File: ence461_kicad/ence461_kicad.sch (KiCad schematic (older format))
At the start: 47 parts, among them U1 LMV324, U2 LMV324, U3 LMV324, U4 74HC3G14DP, U5 LMV321

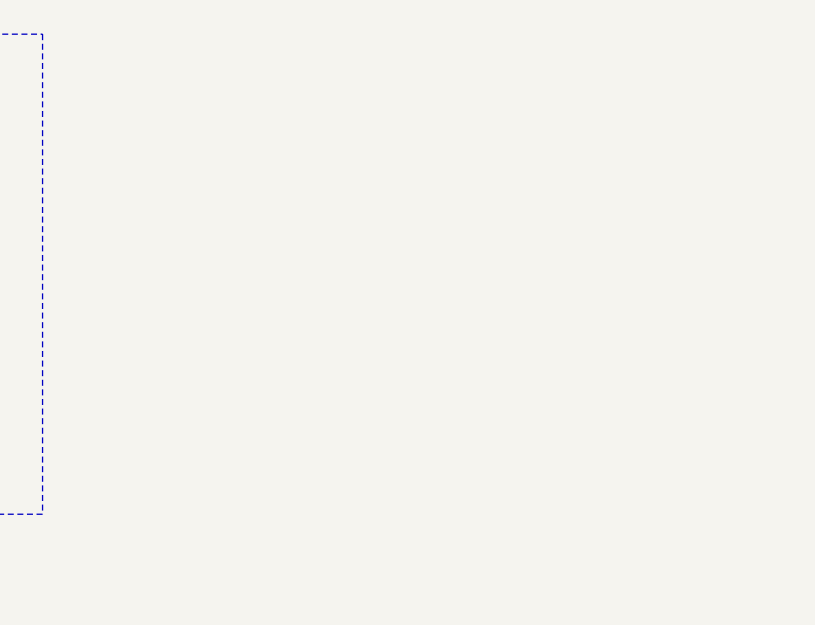
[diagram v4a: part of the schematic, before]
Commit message: Added TPS717 symbol to schematic.
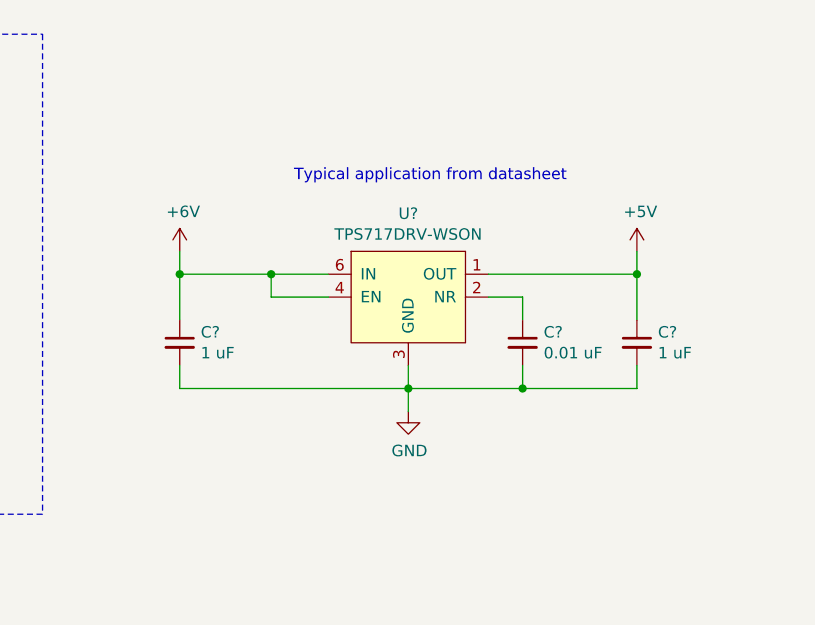
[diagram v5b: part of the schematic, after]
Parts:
- added C?: 0.01 uF, symbol Device:C_Small
- added C? (x2): 1 uF, symbol Device:C_Small
- added U?: TPS717DRV-WSON, Package_SON:WSON-6-1EP_2x2mm_P0.65mm_EP1x1.6mm_ThermalVias, symbol ence461_symbol_library:TPS717DRV-WSON
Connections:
- net +5V: now also C?.1, U?.1 (OUT)
- net GND: now also C?.2, C?.2, C?.2, U?.3 (GND)
- new net: C?.1, U?.2 (NR)
- new net +6V: C?.1, U?.4 (EN), U?.6 (IN)
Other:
- note added: "Typical application from datasheet"
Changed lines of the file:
@@
 Text Notes 3350 11050 0    101  ~ 0
 CAN Transceiver Circuit
+$Comp
+L ence461_symbol_library:TPS717DRV-WSON U?
+U 1 1 5F0550EF
+P 8000 9950
+F 0 "U?" H 8000 10065 50  0000 C CNN
+F 1 "TPS717DRV-WSON" H 8000 9974 50  0000 C CNN
+F 2 "Package_SON:WSON-6-1EP_2x2mm_P0.65mm_EP1x1.6mm_ThermalVias" H 8000 9950 50  0001 C CNN
+F 3 "http://www.ti.com/lit/ds/symlink/tps717.pdf?HQS=TI-null-null-digikeymode-df-pf-null-wwe&ts=1590186425971" H 8000 9950 50  0001 C CNN
+	1    8000 9950
+	1    0    0    -1
+$EndComp
+$Comp
+L power:GND #PWR?
+U 1 1 5F0554ED
+P 8000 10700
+F 0 "#PWR?" H 8000 10450 50  0001 C CNN
+F 1 "GND" H 8005 10527 50  0000 C CNN
+F 2 "" H 8000 10700 50  0001 C CNN
+F 3 "" H 8000 10700 50  0001 C CNN
+	1    8000 10700
+	1    0    0    -1
+$EndComp
+$Comp
+L Device:C_Small C?
+U 1 1 5F05E77E
+P 8500 10400
+F 0 "C?" H 8592 10446 50  0000 L CNN
+F 1 "0.01 uF" H 8592 10355 50  0000 L CNN
+F 2 "" H 8500 10400 50  0001 C CNN
+F 3 "~" H 8500 10400 50  0001 C CNN
+	1    8500 10400
+	1    0    0    -1
+$EndComp
+$Comp
+L Device:C_Small C?
+U 1 1 5F05EC29
+P 7000 10400
+F 0 "C?" H 7092 10446 50  0000 L CNN
+F 1 "1 uF" H 7092 10355 50  0000 L CNN
+F 2 "" H 7000 10400 50  0001 C CNN
+F 3 "~" H 7000 10400 50  0001 C CNN
+	1    7000 10400
+	1    0    0    -1
+$EndComp
+$Comp
+L Device:C_Small C?
+U 1 1 5F05F1F3
+P 9000 10400
+F 0 "C?" H 9092 10446 50  0000 L CNN
+F 1 "1 uF" H 9092 10355 50  0000 L CNN
+F 2 "" H 9000 10400 50  0001 C CNN
+F 3 "~" H 9000 10400 50  0001 C CNN
+	1    9000 10400
+	1    0    0    -1
+$EndComp
+Wire Wire Line
+	8350 10200 8500 10200
+Wire Wire Line
+	8500 10200 8500 10300
+Wire Wire Line
+	8350 10100 9000 10100
+Wire Wire Line
+	8000 10500 8000 10600
+Wire Wire Line
+	8000 10600 8500 10600
+Wire Wire Line
+	8500 10600 8500 10500
+Connection ~ 8000 10600
+Wire Wire Line
+	8000 10600 8000 10700
+Wire Wire Line
+	8500 10600 9000 10600
+Connection ~ 8500 10600
+Wire Wire Line
+	8000 10600 7000 10600
+Wire Wire Line
+	7000 10600 7000 10500
+Wire Wire Line
+	7650 10100 7400 10100
+Wire Wire Line
+	7000 10100 7000 10300
+Wire Wire Line
+	9000 10500 9000 10600
+Wire Wire Line
+	9000 10300 9000 10100
+Wire Wire Line
+	7650 10200 7400 10200
+Wire Wire Line
+	7400 10200 7400 10100
+Connection ~ 7400 10100
+Wire Wire Line
+	7400 10100 7000 10100
+$Comp
+L power:+6V #PWR?
+U 1 1 5F0FB207
+P 7000 10000
+F 0 "#PWR?" H 7000 9850 50  0001 C CNN
+F 1 "+6V" H 7015 10173 50  0000 C CNN
+F 2 "" H 7000 10000 50  0001 C CNN
+F 3 "" H 7000 10000 50  0001 C CNN
+	1    7000 10000
+	1    0    0    -1
+$EndComp
+$Comp
+L power:+5V #PWR?
+U 1 1 5F0FB4D8
+P 9000 10000
+F 0 "#PWR?" H 9000 9850 50  0001 C CNN
+F 1 "+5V" H 9015 10173 50  0000 C CNN
+F 2 "" H 9000 10000 50  0001 C CNN
+F 3 "" H 9000 10000 50  0001 C CNN
+	1    9000 10000
+	1    0    0    -1
+$EndComp
+Wire Wire Line
+	9000 10000 9000 10100
+Connection ~ 9000 10100
+Wire Wire Line
+	7000 10000 7000 10100
+Connection ~ 7000 10100
+Text Notes 7500 9700 0    50   ~ 0
+Typical application from datasheet
 $EndSCHEMATC

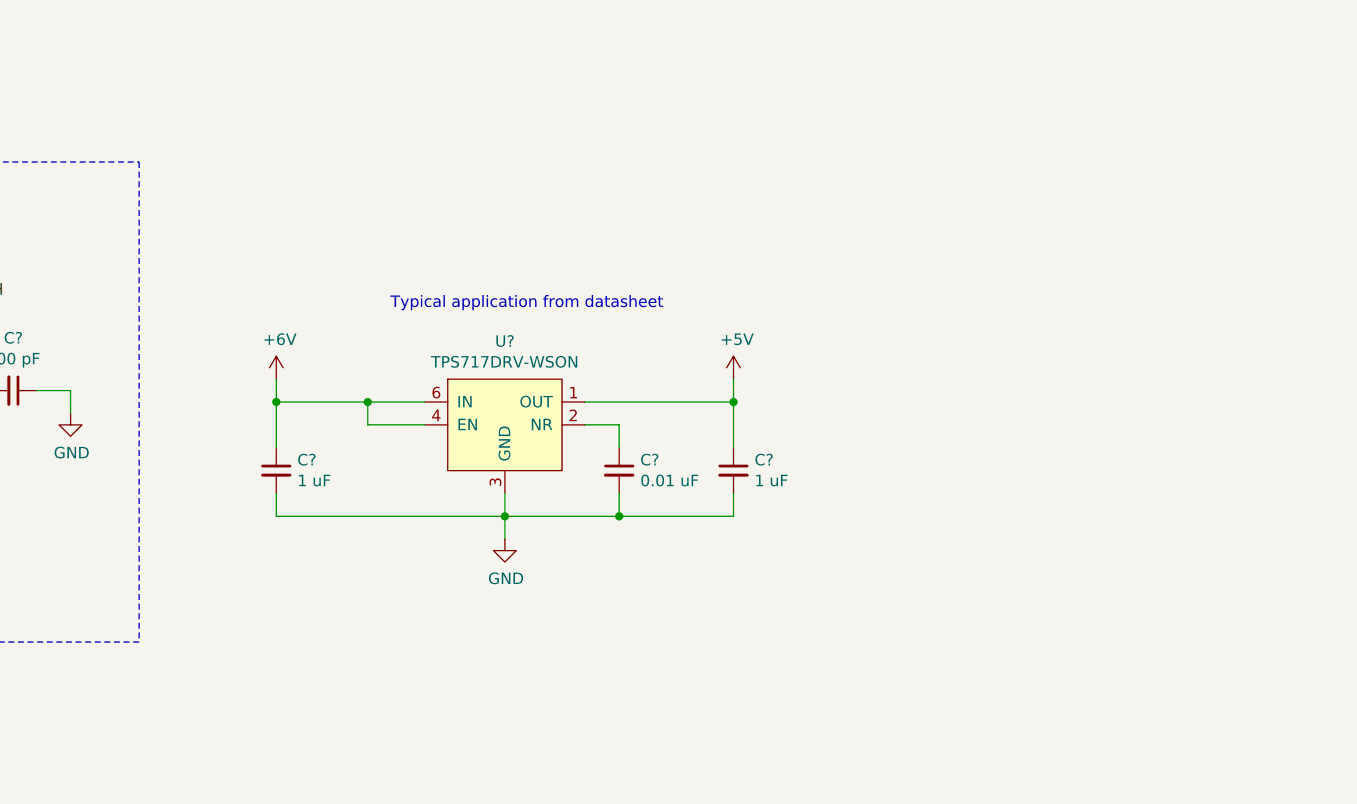
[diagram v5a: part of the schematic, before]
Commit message: Added TPS714 supply.
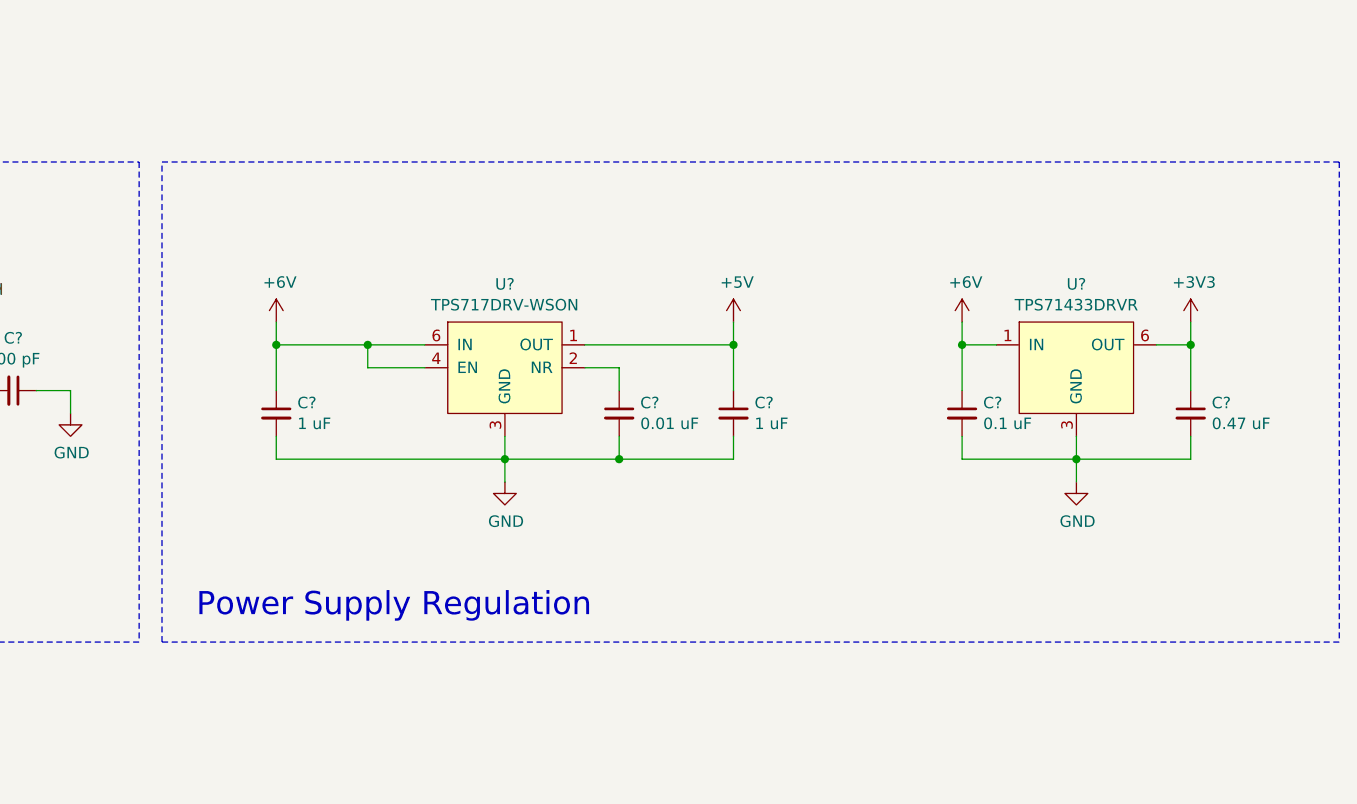
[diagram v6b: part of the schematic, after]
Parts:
- added C?: 0.1 uF, symbol Device:C_Small
- added C?: 0.47 uF, symbol Device:C_Small
- added U?: TPS71433DRVR, Package_SON:WSON-6-1EP_2x2mm_P0.65mm_EP1x1.6mm, symbol ence461_symbol_library:TPS71433DRVR
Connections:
- net +3V3: now also C?.1, U?.6 (OUT)
- net +6V: now also C?.1, U?.1 (IN)
- net GND: now also C?.2, C?.2, U?.3 (GND)
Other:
- note added: "Power Supply Regulation"
- note removed: "Typical application from datasheet"
- moved on the sheet: C?, U?
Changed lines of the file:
@@
 L ence461_symbol_library:TPS717DRV-WSON U?
 U 1 1 5F0550EF
-P 8000 9950
-F 0 "U?" H 8000 10065 50  0000 C CNN
-F 1 "TPS717DRV-WSON" H 8000 9974 50  0000 C CNN
-F 2 "Package_SON:WSON-6-1EP_2x2mm_P0.65mm_EP1x1.6mm_ThermalVias" H 8000 9950 50  0001 C CNN
-F 3 "http://www.ti.com/lit/ds/symlink/tps717.pdf?HQS=TI-null-null-digikeymode-df-pf-null-wwe&ts=1590186425971" H 8000 9950 50  0001 C CNN
-	1    8000 9950
+P 8000 9700
+F 0 "U?" H 8000 9815 50  0000 C CNN
+F 1 "TPS717DRV-WSON" H 8000 9724 50  0000 C CNN
+F 2 "Package_SON:WSON-6-1EP_2x2mm_P0.65mm_EP1x1.6mm_ThermalVias" H 8000 9700 50  0001 C CNN
+F 3 "http://www.ti.com/lit/ds/symlink/tps717.pdf?HQS=TI-null-null-digikeymode-df-pf-null-wwe&ts=1590186425971" H 8000 9700 50  0001 C CNN
+	1    8000 9700
 	1    0    0    -1
 $EndComp
@@
 L power:GND #PWR?
 U 1 1 5F0554ED
-P 8000 10700
-F 0 "#PWR?" H 8000 10450 50  0001 C CNN
-F 1 "GND" H 8005 10527 50  0000 C CNN
-F 2 "" H 8000 10700 50  0001 C CNN
-F 3 "" H 8000 10700 50  0001 C CNN
-	1    8000 10700
+P 8000 10450
+F 0 "#PWR?" H 8000 10200 50  0001 C CNN
+F 1 "GND" H 8005 10277 50  0000 C CNN
+F 2 "" H 8000 10450 50  0001 C CNN
+F 3 "" H 8000 10450 50  0001 C CNN
+	1    8000 10450
 	1    0    0    -1
 $EndComp
@@
 L Device:C_Small C?
 U 1 1 5F05E77E
-P 8500 10400
-F 0 "C?" H 8592 10446 50  0000 L CNN
-F 1 "0.01 uF" H 8592 10355 50  0000 L CNN
-F 2 "" H 8500 10400 50  0001 C CNN
-F 3 "~" H 8500 10400 50  0001 C CNN
-	1    8500 10400
+P 8500 10150
+F 0 "C?" H 8592 10196 50  0000 L CNN
+F 1 "0.01 uF" H 8592 10105 50  0000 L CNN
+F 2 "" H 8500 10150 50  0001 C CNN
+F 3 "~" H 8500 10150 50  0001 C CNN
+	1    8500 10150
 	1    0    0    -1
 $EndComp
@@
 L Device:C_Small C?
 U 1 1 5F05EC29
-P 7000 10400
-F 0 "C?" H 7092 10446 50  0000 L CNN
-F 1 "1 uF" H 7092 10355 50  0000 L CNN
-F 2 "" H 7000 10400 50  0001 C CNN
-F 3 "~" H 7000 10400 50  0001 C CNN
-	1    7000 10400
+P 7000 10150
+F 0 "C?" H 7092 10196 50  0000 L CNN
+F 1 "1 uF" H 7092 10105 50  0000 L CNN
+F 2 "" H 7000 10150 50  0001 C CNN
+F 3 "~" H 7000 10150 50  0001 C CNN
+	1    7000 10150
 	1    0    0    -1
 $EndComp
@@
 L Device:C_Small C?
 U 1 1 5F05F1F3
-P 9000 10400
-F 0 "C?" H 9092 10446 50  0000 L CNN
-F 1 "1 uF" H 9092 10355 50  0000 L CNN
-F 2 "" H 9000 10400 50  0001 C CNN
-F 3 "~" H 9000 10400 50  0001 C CNN
-	1    9000 10400
-	1    0    0    -1
-$EndComp
-Wire Wire Line
-	8350 10200 8500 10200
-Wire Wire Line
-	8500 10200 8500 10300
-Wire Wire Line
-	8350 10100 9000 10100
-Wire Wire Line
-	8000 10500 8000 10600
-Wire Wire Line
-	8000 10600 8500 10600
-Wire Wire Line
-	8500 10600 8500 10500
-Connection ~ 8000 10600
-Wire Wire Line
-	8000 10600 8000 10700
-Wire Wire Line
-	8500 10600 9000 10600
-Connection ~ 8500 10600
-Wire Wire Line
-	8000 10600 7000 10600
-Wire Wire Line
-	7000 10600 7000 10500
-Wire Wire Line
-	7650 10100 7400 10100
-Wire Wire Line
-	7000 10100 7000 10300
-Wire Wire Line
-	9000 10500 9000 10600
-Wire Wire Line
-	9000 10300 9000 10100
-Wire Wire Line
-	7650 10200 7400 10200
-Wire Wire Line
-	7400 10200 7400 10100
-Connection ~ 7400 10100
-Wire Wire Line
-	7400 10100 7000 10100
+P 9000 10150
+F 0 "C?" H 9092 10196 50  0000 L CNN
+F 1 "1 uF" H 9092 10105 50  0000 L CNN
+F 2 "" H 9000 10150 50  0001 C CNN
+F 3 "~" H 9000 10150 50  0001 C CNN
+	1    9000 10150
+	1    0    0    -1
+$EndComp
+Wire Wire Line
+	8350 9950 8500 9950
+Wire Wire Line
+	8500 9950 8500 10050
+Wire Wire Line
+	8350 9850 9000 9850
+Wire Wire Line
+	8000 10250 8000 10350
+Wire Wire Line
+	8000 10350 8500 10350
+Wire Wire Line
+	8500 10350 8500 10250
+Connection ~ 8000 10350
+Wire Wire Line
+	8000 10350 8000 10450
+Wire Wire Line
+	8500 10350 9000 10350
+Connection ~ 8500 10350
+Wire Wire Line
+	8000 10350 7000 10350
+Wire Wire Line
+	7000 10350 7000 10250
+Wire Wire Line
+	7650 9850 7400 9850
+Wire Wire Line
+	7000 9850 7000 10050
+Wire Wire Line
+	9000 10250 9000 10350
+Wire Wire Line
+	9000 10050 9000 9850
+Wire Wire Line
+	7650 9950 7400 9950
+Wire Wire Line
+	7400 9950 7400 9850
+Connection ~ 7400 9850
+Wire Wire Line
+	7400 9850 7000 9850
 $Comp
 L power:+6V #PWR?
 U 1 1 5F0FB207
-P 7000 10000
-F 0 "#PWR?" H 7000 9850 50  0001 C CNN
-F 1 "+6V" H 7015 10173 50  0000 C CNN
-F 2 "" H 7000 10000 50  0001 C CNN
-F 3 "" H 7000 10000 50  0001 C CNN
-	1    7000 10000
+P 7000 9750
+F 0 "#PWR?" H 7000 9600 50  0001 C CNN
+F 1 "+6V" H 7015 9923 50  0000 C CNN
+F 2 "" H 7000 9750 50  0001 C CNN
+F 3 "" H 7000 9750 50  0001 C CNN
+	1    7000 9750
 	1    0    0    -1
 $EndComp
@@
 L power:+5V #PWR?
 U 1 1 5F0FB4D8
-P 9000 10000
-F 0 "#PWR?" H 9000 9850 50  0001 C CNN
-F 1 "+5V" H 9015 10173 50  0000 C CNN
-F 2 "" H 9000 10000 50  0001 C CNN
-F 3 "" H 9000 10000 50  0001 C CNN
-	1    9000 10000
-	1    0    0    -1
-$EndComp
-Wire Wire Line
-	9000 10000 9000 10100
-Connection ~ 9000 10100
-Wire Wire Line
-	7000 10000 7000 10100
-Connection ~ 7000 10100
-Text Notes 7500 9700 0    50   ~ 0
-Typical application from datasheet
+P 9000 9750
+F 0 "#PWR?" H 9000 9600 50  0001 C CNN
+F 1 "+5V" H 9015 9923 50  0000 C CNN
+F 2 "" H 9000 9750 50  0001 C CNN
+F 3 "" H 9000 9750 50  0001 C CNN
+	1    9000 9750
+	1    0    0    -1
+$EndComp
+Wire Wire Line
+	9000 9750 9000 9850
+Connection ~ 9000 9850
+Wire Wire Line
+	7000 9750 7000 9850
+Connection ~ 7000 9850
+$Comp
+L ence461_symbol_library:TPS71433DRVR U?
+U 1 1 5F130B93
+P 10500 9700
+F 0 "U?" H 10500 9815 50  0000 C CNN
+F 1 "TPS71433DRVR" H 10500 9724 50  0000 C CNN
+F 2 "Package_SON:WSON-6-1EP_2x2mm_P0.65mm_EP1x1.6mm" H 10500 9700 50  0001 C CNN
+F 3 "http://www.ti.com/lit/ds/symlink/tps714.pdf?HQS=TI-null-null-digikeymode-df-pf-null-wwe&ts=1590190303413" H 10500 9700 50  0001 C CNN
+	1    10500 9700
+	1    0    0    -1
+$EndComp
+$Comp
+L Device:C_Small C?
+U 1 1 5F1319AF
+P 10000 10150
+F 0 "C?" H 10092 10196 50  0000 L CNN
+F 1 "0.1 uF" H 10092 10105 50  0000 L CNN
+F 2 "" H 10000 10150 50  0001 C CNN
+F 3 "~" H 10000 10150 50  0001 C CNN
+	1    10000 10150
+	1    0    0    -1
+$EndComp
+$Comp
+L Device:C_Small C?
+U 1 1 5F131C86
+P 11000 10150
+F 0 "C?" H 11092 10196 50  0000 L CNN
+F 1 "0.47 uF" H 11092 10105 50  0000 L CNN
+F 2 "" H 11000 10150 50  0001 C CNN
+F 3 "~" H 11000 10150 50  0001 C CNN
+	1    11000 10150
+	1    0    0    -1
+$EndComp
+Wire Wire Line
+	11000 10050 11000 9850
+Wire Wire Line
+	11000 9850 10850 9850
+Wire Wire Line
+	11000 10250 11000 10350
+Wire Wire Line
+	11000 10350 10500 10350
+Wire Wire Line
+	10500 10350 10500 10250
+Wire Wire Line
+	10000 10050 10000 9850
+Wire Wire Line
+	10000 9850 10150 9850
+Wire Wire Line
+	10000 10250 10000 10350
+Wire Wire Line
+	10000 10350 10500 10350
+Connection ~ 10500 10350
+$Comp
+L power:GND #PWR?
+U 1 1 5F1611CF
+P 10500 10450
+F 0 "#PWR?" H 10500 10200 50  0001 C CNN
+F 1 "GND" H 10505 10277 50  0000 C CNN
+F 2 "" H 10500 10450 50  0001 C CNN
+F 3 "" H 10500 10450 50  0001 C CNN
+	1    10500 10450
+	1    0    0    -1
+$EndComp
+Wire Wire Line
+	10500 10450 10500 10350
+$Comp
+L power:+3V3 #PWR?
+U 1 1 5F16C988
+P 11000 9750
+F 0 "#PWR?" H 11000 9600 50  0001 C CNN
+F 1 "+3V3" H 11015 9923 50  0000 C CNN
+F 2 "" H 11000 9750 50  0001 C CNN
+F 3 "" H 11000 9750 50  0001 C CNN
+	1    11000 9750
+	1    0    0    -1
+$EndComp
+Wire Wire Line
+	11000 9750 11000 9850
+Connection ~ 11000 9850
+$Comp
+L power:+6V #PWR?
+U 1 1 5F1792AF
+P 10000 9750
+F 0 "#PWR?" H 10000 9600 50  0001 C CNN
+F 1 "+6V" H 10015 9923 50  0000 C CNN
+F 2 "" H 10000 9750 50  0001 C CNN
+F 3 "" H 10000 9750 50  0001 C CNN
+	1    10000 9750
+	1    0    0    -1
+$EndComp
+Wire Wire Line
+	10000 9750 10000 9850
+Connection ~ 10000 9850
+Wire Notes Line
+	6500 11150 6500 9050
+Wire Notes Line
+	6500 9050 11650 9050
+Wire Notes Line
+	11650 9050 11650 11150
+Wire Notes Line
+	11650 11150 6500 11150
+Text Notes 6650 11050 0    101  ~ 0
+Power Supply Regulation
 $EndSCHEMATC
